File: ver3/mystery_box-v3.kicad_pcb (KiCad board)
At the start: 2 copper layers, 136 x 100 mm, 61 parts, among them J1 Screw_Terminal_01x02, J10 Screw_Terminal_01x02, J11 Screw_Terminal_01x02, J12 Screw_Terminal_01x02, J13 Screw_Terminal_01x02, J14 Screw_Terminal_01x02, J15 Screw_Terminal_01x02, J16 Screw_Terminal_01x02, J17 Screw_Terminal_01x02, J18 Barrel_Jack_MountingPin, J20 rj45-CC-X2-Aliexpress, J3 SERIAL1, J8 Screw_Terminal_01x02, J9 Screw_Terminal_01x02, Q1 IRLZ44N, Q2 IRLZ44N, Q3 IRLZ44N, SW01 Screw_Terminal_01x02, SW02 Screw_Terminal_01x02, SW03 Screw_Terminal_01x02, U1 THVD1400D

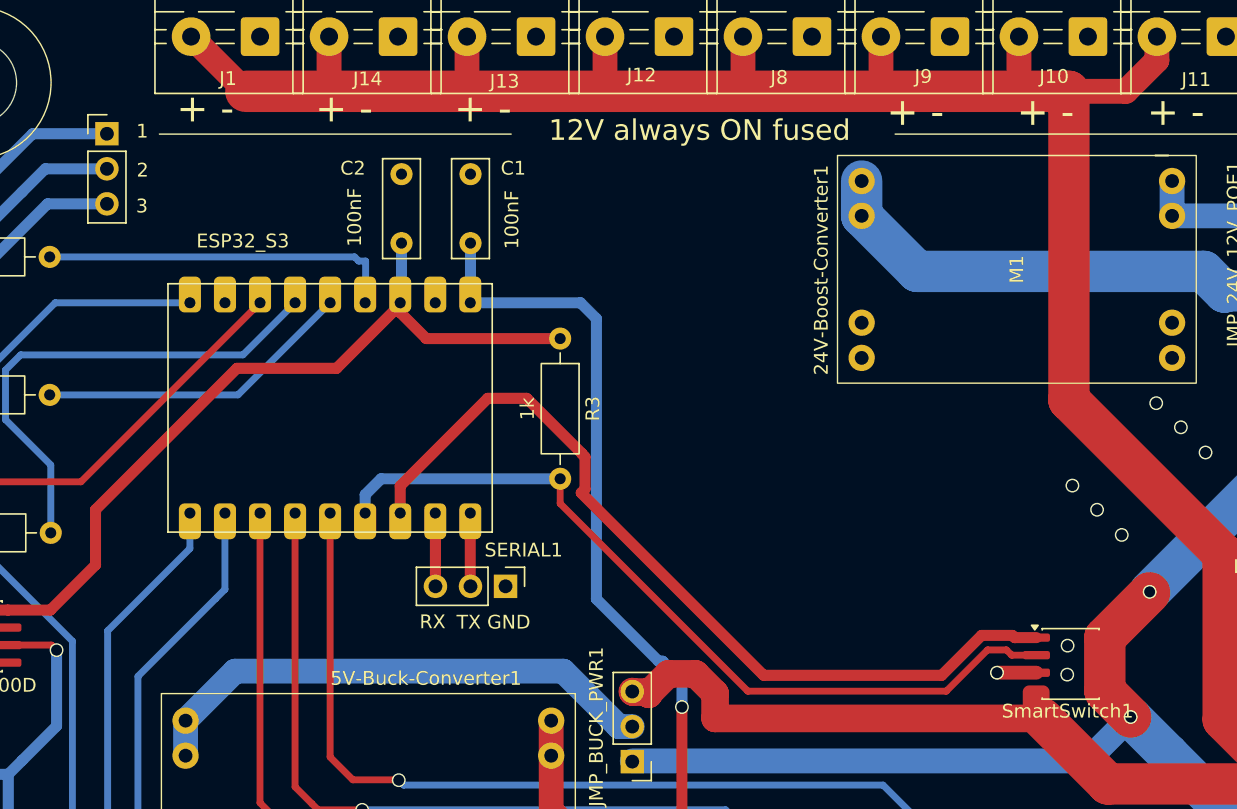
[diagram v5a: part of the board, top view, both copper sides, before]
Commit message: fixed SmartSwitch Pad
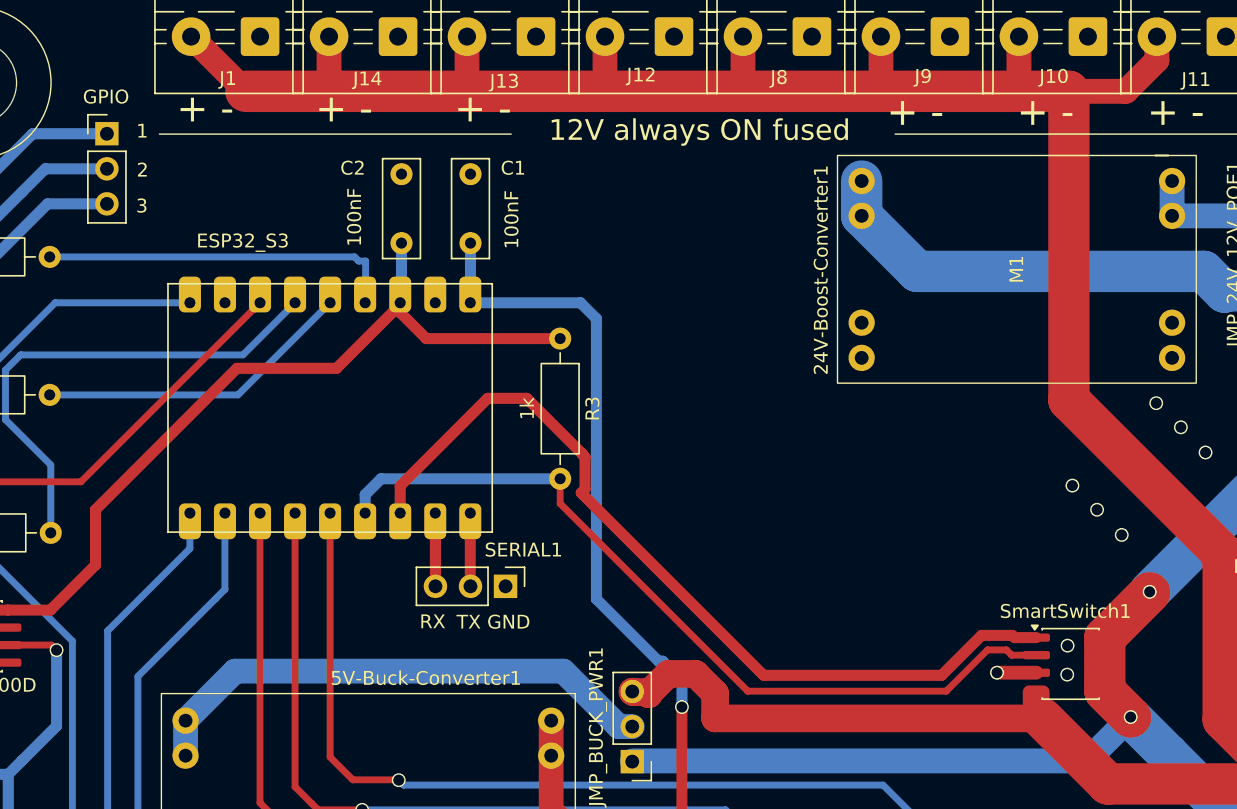
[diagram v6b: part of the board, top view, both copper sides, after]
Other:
- board text added: "GPIO"
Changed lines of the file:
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@@
 		(tags "SOIC SO")
 		(property "Reference" "SmartSwitch1"
-			(at -0.225 3.425 0)
+			(at -0.375 -3.8 0)
 			(layer "F.SilkS")
 			(effects
@@
 			(at -2.5 3.02625)
 			(size 1.95 2.9475)
-			(layers "F.Cu" "F.Mask" "F.Paste")
+			(layers "F.Cu")
 			(roundrect_rratio 0.25)
 			(net 4 "VCC 12V SW")
@@
 		)
 	)
+	(gr_text "GPIO"
+		(at 161.4 34 0)
+		(layer "F.SilkS")
+		(effects
+			(font
+				(size 1 1)
+				(thickness 0.1)
+			)
+			(justify left bottom)
+		)
+	)
 	(gr_text "2"
 		(at 165.3 39.3 0)
@@
 			)
 		)
+	)
+	(zone
+		(net 0)
+		(net_name "")
+		(layer "F.Mask")
+		(hatch edge 0.5)
+		(connect_pads
+			(clearance 1)
+		)
+		(min_thickness 0.25)
+		(filled_areas_thickness no)
+		(fill yes
+			(thermal_gap 0.5)
+			(thermal_bridge_width 0.5)
+			(smoothing fillet)
+			(radius 2)
+		)
+		(polygon
+			(pts
+				(xy 229.525 76.075) (xy 231.475 76.075) (xy 231.475 76.875) (xy 229.525 76.875)
+			)
+		)
